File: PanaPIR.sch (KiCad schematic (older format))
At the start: 3 parts, among them P1 HEADER, P2 HEADER, U1 PIR

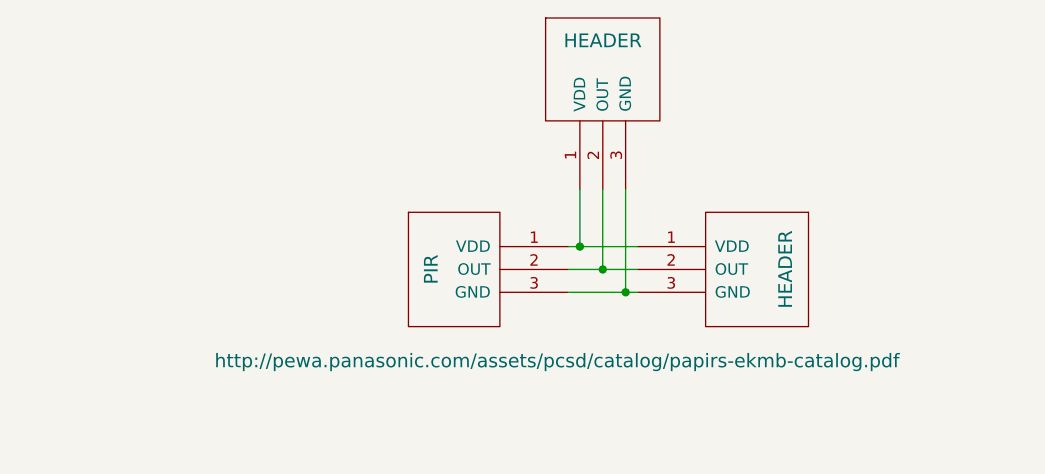
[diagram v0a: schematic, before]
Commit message: Add 0603 decoupling cap and better spacing for breadboards
600 mil center drill distance from top to bottom for PTH headers.
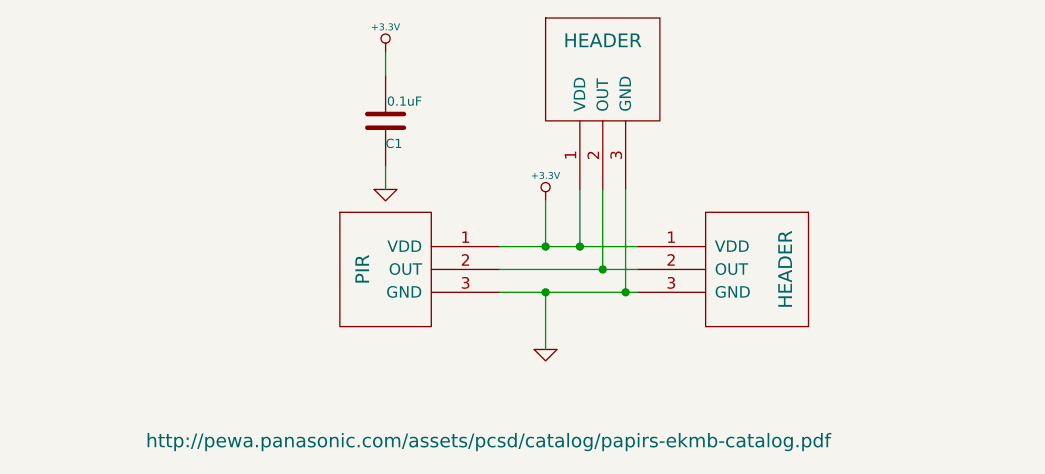
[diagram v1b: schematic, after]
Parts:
- added C1: 0.1uF, ~, symbol C
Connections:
- net +3.3V: now reaches P1.1 (VDD), P2.1 (VDD), U1.1 (VDD)
- net +3.3V: now also C1.2
- net GND: now reaches P1.3 (GND), P2.3 (GND), U1.3 (GND)
- net GND: now also C1.1
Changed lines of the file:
@@
 Sheet 1 1
 Title ""
-Date "18 feb 2014"
+Date "9 apr 2014"
 Rev ""
 Comp ""
@@
 L PIR U1
 U 1 1 52FDB02B
-P 5050 4650
-F 0 "U1" H 5000 4550 60  0001 C CNN
-F 1 "PIR" V 4900 4750 60  0000 C CNN
-F 2 "" H 5050 4650 60  0000 C CNN
-F 3 "http://pewa.panasonic.com/assets/pcsd/catalog/papirs-ekmb-catalog.pdf" H 5450 4350 60  0000 C CNN
-	1    5050 4650
+P 4750 4650
+F 0 "U1" H 4700 4550 60  0001 C CNN
+F 1 "PIR" V 4600 4750 60  0000 C CNN
+F 2 "" H 4750 4650 60  0000 C CNN
+F 3 "http://pewa.panasonic.com/assets/pcsd/catalog/papirs-ekmb-catalog.pdf" H 5150 4000 60  0000 C CNN
+	1    4750 4650
 	1    0    0    -1
 $EndComp
@@
 $EndComp
 Wire Wire Line
-	5500 4450 5800 4450
+	5200 4450 5800 4450
 Wire Wire Line
-	5800 4550 5500 4550
+	5200 4550 5800 4550
 Wire Wire Line
-	5500 4650 5800 4650
+	5200 4650 5800 4650
 $Comp
 L HEADER P1
@@
 	1    0    0    -1
 $EndComp
-Wire Wire Line
-	5550 4200 5550 4450
 Connection ~ 5550 4450
 Wire Wire Line
@@
 	5750 4200 5750 4650
 Connection ~ 5750 4650
+$Comp
+L C C1
+U 1 1 53448E7D
+P 4700 3900
+F 0 "C1" H 4700 4000 40  0000 L CNN
+F 1 "0.1uF" H 4706 3815 40  0000 L CNN
+F 2 "~" H 4738 3750 30  0000 C CNN
+F 3 "~" H 4700 3900 60  0000 C CNN
+	1    4700 3900
+	1    0    0    1
+$EndComp
+$Comp
+L +3.3V #PWR01
+U 1 1 53448EAC
+P 5400 4250
+F 0 "#PWR01" H 5400 4210 30  0001 C CNN
+F 1 "+3.3V" H 5400 4360 30  0000 C CNN
+F 2 "" H 5400 4250 60  0000 C CNN
+F 3 "" H 5400 4250 60  0000 C CNN
+	1    5400 4250
+	1    0    0    -1
+$EndComp
+$Comp
+L GND #PWR02
+U 1 1 53448EC2
+P 5400 4900
+F 0 "#PWR02" H 5400 4900 30  0001 C CNN
+F 1 "GND" H 5400 4830 30  0001 C CNN
+F 2 "" H 5400 4900 60  0000 C CNN
+F 3 "" H 5400 4900 60  0000 C CNN
+	1    5400 4900
+	1    0    0    -1
+$EndComp
+Wire Wire Line
+	5400 4250 5400 4450
+Wire Wire Line
+	5400 4650 5400 4900
+Connection ~ 5400 4650
+Wire Wire Line
+	5550 4200 5550 4450
+Connection ~ 5400 4450
+$Comp
+L +3.3V #PWR03
+U 1 1 53448FC4
+P 4700 3600
+F 0 "#PWR03" H 4700 3560 30  0001 C CNN
+F 1 "+3.3V" H 4700 3710 30  0000 C CNN
+F 2 "" H 4700 3600 60  0000 C CNN
+F 3 "" H 4700 3600 60  0000 C CNN
+	1    4700 3600
+	1    0    0    -1
+$EndComp
+$Comp
+L GND #PWR04
+U 1 1 53448FCA
+P 4700 4200
+F 0 "#PWR04" H 4700 4200 30  0001 C CNN
+F 1 "GND" H 4700 4130 30  0001 C CNN
+F 2 "" H 4700 4200 60  0000 C CNN
+F 3 "" H 4700 4200 60  0000 C CNN
+	1    4700 4200
+	1    0    0    -1
+$EndComp
+Wire Wire Line
+	4700 3600 4700 3700
+Wire Wire Line
+	4700 4200 4700 4100
 $EndSCHEMATC
